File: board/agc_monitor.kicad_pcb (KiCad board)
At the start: 2 copper layers, 3 parts, among them J3 Conn_04x24, J4 Conn_04x24, P1 test_connector

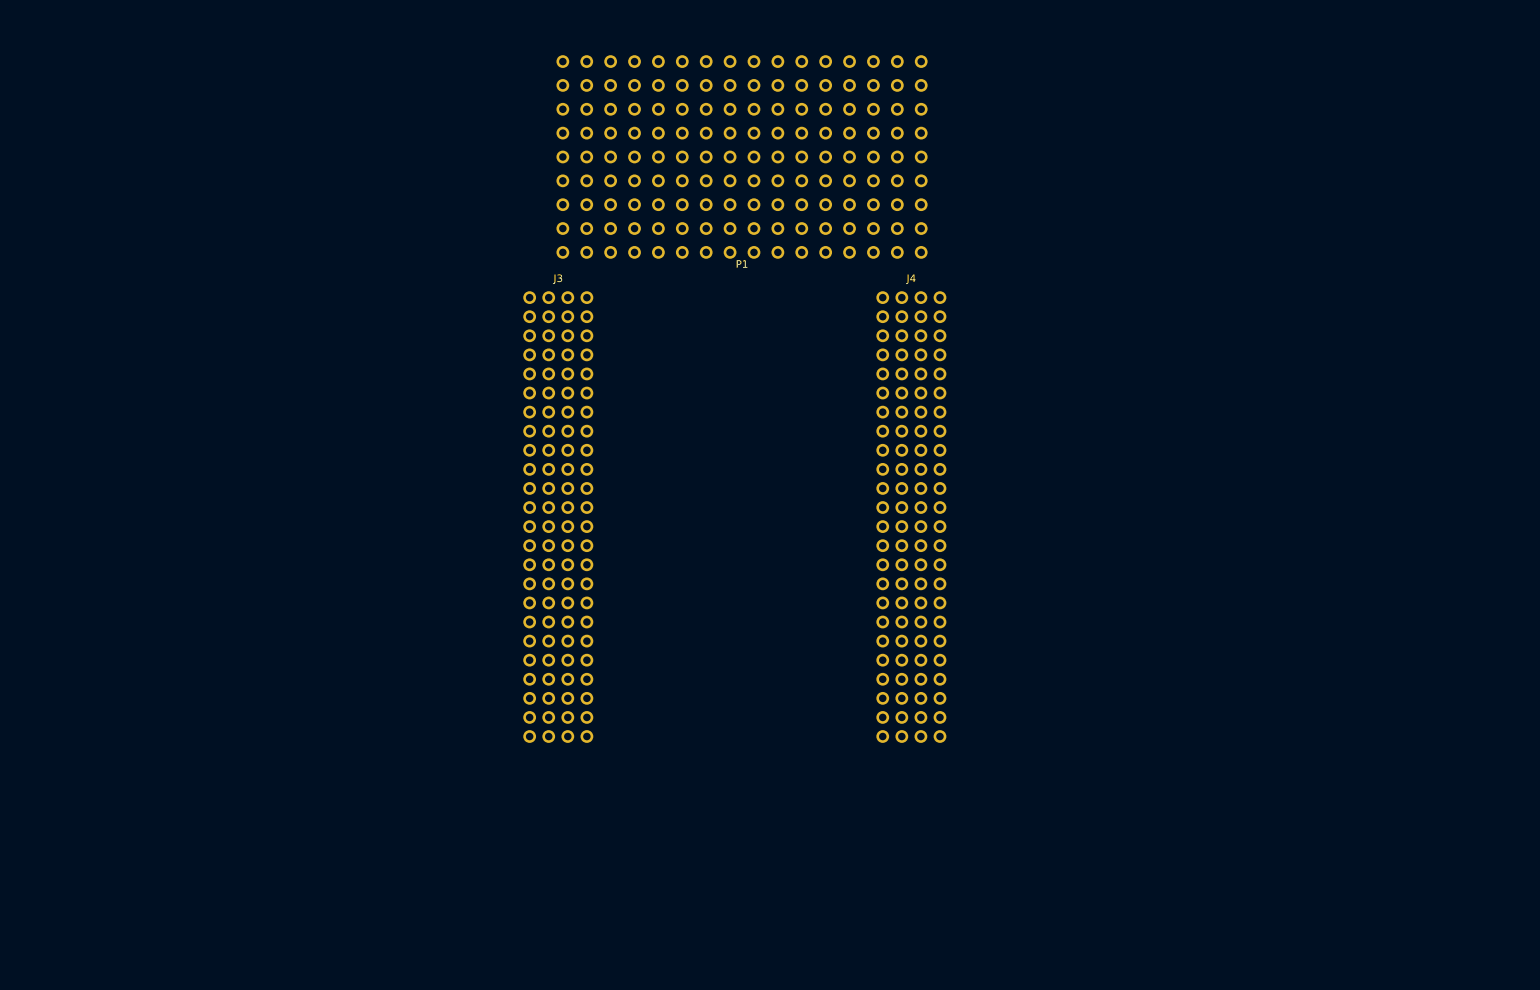
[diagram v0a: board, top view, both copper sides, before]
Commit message: Board: minor schematic tweaks, footprint creation, and initial subcircuit layout
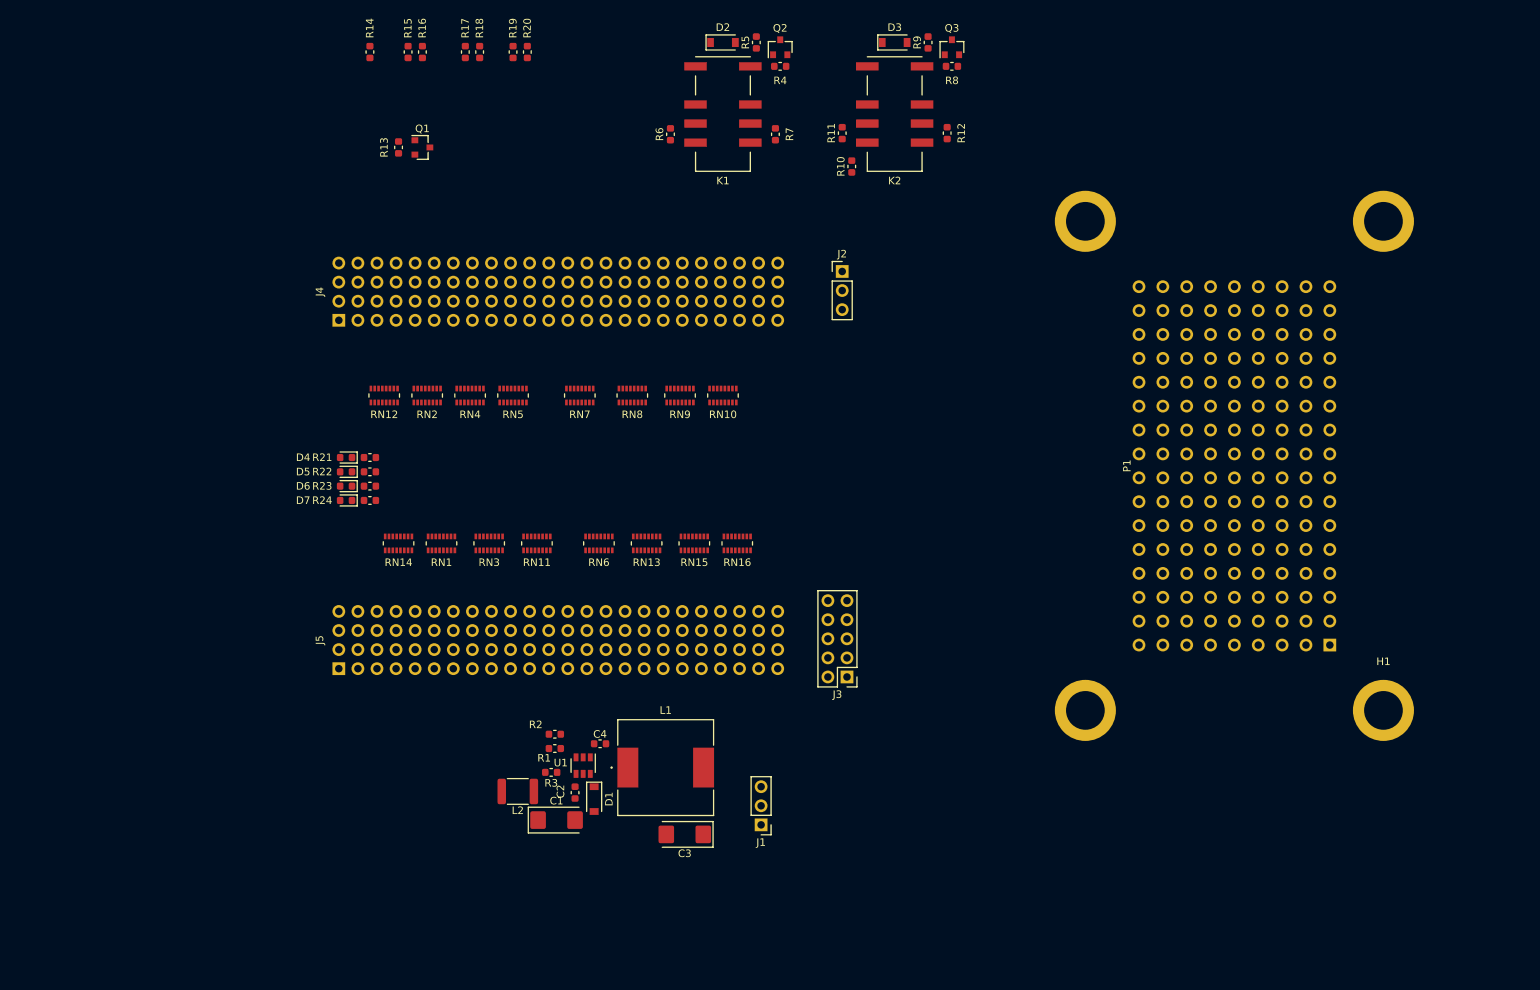
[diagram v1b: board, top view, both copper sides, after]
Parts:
- added C1: 6.8uF, Capacitor_Tantalum_SMD:CP_EIA-6032-28_Kemet-C, F.Cu at (99.8, 140.3)
- added C2: 4.7uF, Capacitor_SMD:C_0603_1608Metric, F.Cu at (102.2, 136.7)
- added C3: 22uF, Capacitor_Tantalum_SMD:CP_EIA-6032-28_Kemet-C, F.Cu at (116.8, 142.2)
- added C4: 100nF, Capacitor_SMD:C_0603_1608Metric, F.Cu at (105.6, 130.2)
- added D1: 30V,500mA, Diode_SMD:D_SOD-123, F.Cu at (104.8, 137.5)
- added D2: D_ALT, Diode_SMD:D_SOD-123, F.Cu at (121.9, 36.8)
- added D3: D_ALT, Diode_SMD:D_SOD-123, F.Cu at (144.8, 36.8)
- added D4: LED, LED_SMD:LED_0603_1608Metric, F.Cu at (71.8, 92.1)
- added D5: LED, LED_SMD:LED_0603_1608Metric, F.Cu at (71.8, 94.0)
- added D6: LED, LED_SMD:LED_0603_1608Metric, F.Cu at (71.8, 95.9)
- added D7: LED, LED_SMD:LED_0603_1608Metric, F.Cu at (71.8, 97.8)
- added H1: MountingHole_Pad, agc_monitor:MountingHole_1004579, F.Cu at (209.8, 125.7)
- added H2: MountingHole_Pad, agc_monitor:MountingHole_1004579, F.Cu at (170.2, 125.7)
- added H3: MountingHole_Pad, agc_monitor:MountingHole_1004579, F.Cu at (170.2, 60.6)
- added H4: MountingHole_Pad, agc_monitor:MountingHole_1004579, F.Cu at (209.8, 60.6)
- added J1: Conn_01x03, Connector_PinHeader_2.54mm:PinHeader_1x03_P2.54mm_Vertical, F.Cu at (127.0, 141.0)
- added J2: Conn_01x03, Connector_PinHeader_2.54mm:PinHeader_1x03_P2.54mm_Vertical, F.Cu at (137.8, 67.3)
- added J5: Styx_P5, agc_monitor:PinHeader_4x24_P2.54mm_Vertical, F.Cu at (100.0, 116.4)
- added K1: EE2-12NU, agc_monitor:Kemet-EE2, F.Cu at (121.9, 46.4)
- added K2: EE2-12NU, agc_monitor:Kemet-EE2, F.Cu at (144.8, 46.4)
- added L1: 68uH, agc_monitor:SRR1210-680M, F.Cu at (114.3, 133.3)
- added L2: 8.2uH, Inductor_SMD:L_1812_4532Metric, F.Cu at (94.6, 136.5)
- added Q1: MMBT3904, Package_TO_SOT_SMD:SOT-23, F.Cu at (81.9, 50.8)
- added Q2: MMBT3904, Package_TO_SOT_SMD:SOT-23, F.Cu at (129.5, 37.5)
- added Q3: MMBT3904, Package_TO_SOT_SMD:SOT-23, F.Cu at (152.4, 37.5)
- added R1: 28k, Resistor_SMD:R_0603_1608Metric, F.Cu at (99.5, 130.8)
- added R10: 3.3k, Resistor_SMD:R_0603_1608Metric, F.Cu at (139.1, 53.3)
- added R11: 0, Resistor_SMD:R_0603_1608Metric, F.Cu at (137.8, 48.9)
- added R12: 0, Resistor_SMD:R_0603_1608Metric, F.Cu at (151.8, 48.9)
- added R13: 1.5k, Resistor_SMD:R_0603_1608Metric, F.Cu at (78.7, 50.8)
- added R14: 1.2k, Resistor_SMD:R_0603_1608Metric, F.Cu at (74.9, 38.1)
- added R15: 4.7k, Resistor_SMD:R_0603_1608Metric, F.Cu at (80.0, 38.1)
- added R16: 1.5k, Resistor_SMD:R_0603_1608Metric, F.Cu at (81.9, 38.1)
- added R17: 4.7k, Resistor_SMD:R_0603_1608Metric, F.Cu at (87.6, 38.1)
- added R18: 1.2k, Resistor_SMD:R_0603_1608Metric, F.Cu at (89.5, 38.1)
- added R19: 22k, Resistor_SMD:R_0603_1608Metric, F.Cu at (94.0, 38.1)
- added R2: 8.45k, Resistor_SMD:R_0603_1608Metric, F.Cu at (99.5, 128.9)
- added R20: 1.5k, Resistor_SMD:R_0603_1608Metric, F.Cu at (95.9, 38.1)
- added R21: 330, Resistor_SMD:R_0603_1608Metric, F.Cu at (74.9, 92.1)
- added R22: 330, Resistor_SMD:R_0603_1608Metric, F.Cu at (74.9, 94.0)
- added R23: 330, Resistor_SMD:R_0603_1608Metric, F.Cu at (74.9, 95.9)
- added R24: 330, Resistor_SMD:R_0603_1608Metric, F.Cu at (74.9, 97.8)
- added R3: 0, Resistor_SMD:R_0603_1608Metric, F.Cu at (99.1, 134.0)
- added R4: 1.5k, Resistor_SMD:R_0603_1608Metric, F.Cu at (129.5, 40.0)
- added R5: 150, Resistor_SMD:R_0603_1608Metric, F.Cu at (126.4, 36.8)
- added R6: 0, Resistor_SMD:R_0603_1608Metric, F.Cu at (114.9, 49.0)
- added R7: 0, Resistor_SMD:R_0603_1608Metric, F.Cu at (128.9, 49.0)
- added R8: 1.5k, Resistor_SMD:R_0603_1608Metric, F.Cu at (152.4, 40.0)
- added R9: 150, Resistor_SMD:R_0603_1608Metric, F.Cu at (149.2, 36.8)
- added RN1: 3.3k, agc_monitor:EXB-2HV332JV, F.Cu at (84.5, 103.5)
- added RN10: 3.3k, agc_monitor:EXB-2HV332JV, F.Cu at (121.9, 83.8)
- added RN11: 3.3k, agc_monitor:EXB-2HV332JV, F.Cu at (97.2, 103.5)
- added RN12: 3.3k, agc_monitor:EXB-2HV332JV, F.Cu at (76.8, 83.8)
- added RN13: 3.3k, agc_monitor:EXB-2HV332JV, F.Cu at (111.8, 103.5)
- added RN14: 3.3k, agc_monitor:EXB-2HV332JV, F.Cu at (78.7, 103.5)
- added RN15: 3.3k, agc_monitor:EXB-2HV332JV, F.Cu at (118.1, 103.5)
- added RN16: 3.3k, agc_monitor:EXB-2HV332JV, F.Cu at (123.8, 103.5)
- added RN2: 3.3k, agc_monitor:EXB-2HV332JV, F.Cu at (82.5, 83.8)
- added RN3: 3.3k, agc_monitor:EXB-2HV332JV, F.Cu at (90.8, 103.5)
- added RN4: 3.3k, agc_monitor:EXB-2HV332JV, F.Cu at (88.3, 83.8)
- added RN5: 3.3k, agc_monitor:EXB-2HV332JV, F.Cu at (94.0, 83.8)
- added RN6: 3.3k, agc_monitor:EXB-2HV332JV, F.Cu at (105.4, 103.5)
- added RN7: 3.3k, agc_monitor:EXB-2HV332JV, F.Cu at (102.9, 83.8)
- added RN8: 3.3k, agc_monitor:EXB-2HV332JV, F.Cu at (109.9, 83.8)
- added RN9: 3.3k, agc_monitor:EXB-2HV332JV, F.Cu at (116.2, 83.8)
- added U1: LMR16006XDDC, Package_TO_SOT_SMD:SOT-23-6, F.Cu at (103.3, 133.1)
- J3: value Conn_04x24 -> Conn_01x10; footprint agc_monitor:PinHeader_4x24_P2.54mm_Vertical -> Connector_PinHeader_2.54mm:PinHeader_2x05_P2.54mm_Vertical
- J4: value Conn_04x24 -> Styx_P4
- moved P1 77.4 mm to (190.0, 93.2), turned to 270 degrees
- moved J4 55.8 mm to (100.0, 70.0), turned to 90 degrees
- moved J3 43.9 mm to (138.4, 121.3), turned to 180 degrees
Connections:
- J3 pad 1: Net-(J3-Pad1) -> +3V3_IO
- J3 pad 10: Net-(J3-Pad10) -> GND
- J3 pad 2: Net-(J3-Pad2) -> /StyxConnectors/DBG1
- J3 pad 3: Net-(J3-Pad3) -> /StyxConnectors/DBG2
- J3 pad 4: Net-(J3-Pad4) -> /StyxConnectors/DBG3
- J3 pad 5: Net-(J3-Pad5) -> /StyxConnectors/DBG4
- J3 pad 6: Net-(J3-Pad6) -> /StyxConnectors/DBG5
- J3 pad 7: Net-(J3-Pad7) -> /StyxConnectors/DBG6
- J3 pad 8: Net-(J3-Pad8) -> /StyxConnectors/DBG7
- J3 pad 9: Net-(J3-Pad9) -> /StyxConnectors/DBG8
- J4 pad 10: Net-(J4-Pad10) -> ADC_BPLSSW_P
- J4 pad 11: Net-(J4-Pad11) -> GND
- J4 pad 12: Net-(J4-Pad12) -> ADC_4SW_P
- J4 pad 13: Net-(J4-Pad13) -> MWCH
- J4 pad 14: Net-(J4-Pad14) -> MRCH
- J4 pad 15: Net-(J4-Pad15) -> GND
- J4 pad 16: Net-(J4-Pad16) -> MTLO
- J4 pad 17: Net-(J4-Pad17) -> MWL01
- J4 pad 18: Net-(J4-Pad18) -> MWL02
- J4 pad 19: Net-(J4-Pad19) -> MWL03
- J4 pad 2: Net-(J4-Pad2) -> +3V3_FPGA
- J4 pad 20: Net-(J4-Pad20) -> MWL04
- J4 pad 21: Net-(J4-Pad21) -> MWL05
- J4 pad 22: Net-(J4-Pad22) -> MWL06
- J4 pad 23: Net-(J4-Pad23) -> MWL07
- J4 pad 24: Net-(J4-Pad24) -> MWL08
- J4 pad 25: Net-(J4-Pad25) -> MWL09
- J4 pad 26: Net-(J4-Pad26) -> MWL10
- J4 pad 27: Net-(J4-Pad27) -> MWL11
- J4 pad 28: Net-(J4-Pad28) -> MWL12
- J4 pad 29: Net-(J4-Pad29) -> MWL13
- J4 pad 30: Net-(J4-Pad30) -> MWL14
- J4 pad 31: Net-(J4-Pad31) -> MWL15
- J4 pad 32: Net-(J4-Pad32) -> MWL16
- J4 pad 33: Net-(J4-Pad33) -> MT01
- J4 pad 34: Net-(J4-Pad34) -> MT02
- J4 pad 35: Net-(J4-Pad35) -> MT03
- J4 pad 36: Net-(J4-Pad36) -> MT04
- J4 pad 37: Net-(J4-Pad37) -> MT05
- J4 pad 38: Net-(J4-Pad38) -> MT06
- J4 pad 39: Net-(J4-Pad39) -> MT07
- J4 pad 4: Net-(J4-Pad4) -> GND
- J4 pad 40: Net-(J4-Pad40) -> MT08
- J4 pad 41: Net-(J4-Pad41) -> MT09
- J4 pad 42: Net-(J4-Pad42) -> MT10
- J4 pad 43: Net-(J4-Pad43) -> MT11
- J4 pad 44: Net-(J4-Pad44) -> MT12
- J4 pad 45: Net-(J4-Pad45) -> Net-(J4-Pad1)
- J4 pad 46: Net-(J4-Pad46) -> ADC_3V3_P
- J4 pad 47: Net-(J4-Pad47) -> /StyxConnectors/DBG1
- J4 pad 48: Net-(J4-Pad48) -> /StyxConnectors/DBG2
- J4 pad 49: Net-(J4-Pad49) -> Net-(J4-Pad1)
- J4 pad 5: Net-(J4-Pad5) -> MWG
- J4 pad 50: Net-(J4-Pad50) -> GND
- J4 pad 51: Net-(J4-Pad51) -> GND
- J4 pad 52: Net-(J4-Pad52) -> GND
- J4 pad 53: Net-(J4-Pad53) -> MST1
- J4 pad 54: Net-(J4-Pad54) -> MST2
- J4 pad 55: Net-(J4-Pad55) -> MST3
- J4 pad 56: Net-(J4-Pad56) -> MTCSA_n
- J4 pad 57: Net-(J4-Pad57) -> MWSG
- J4 pad 58: Net-(J4-Pad58) -> MWZG
- J4 pad 59: Net-(J4-Pad59) -> MWYG
- J4 pad 6: Net-(J4-Pad6) -> MNISQ
- J4 pad 60: Net-(J4-Pad60) -> MWQG
- J4 pad 61: Net-(J4-Pad61) -> MWBG
- J4 pad 62: Net-(J4-Pad62) -> MSQ10
- J4 pad 63: Net-(J4-Pad63) -> MSQ11
- J4 pad 64: Net-(J4-Pad64) -> MSQ12
- J4 pad 65: Net-(J4-Pad65) -> MSQ13
- J4 pad 66: Net-(J4-Pad66) -> MSQ14
- J4 pad 67: Net-(J4-Pad67) -> MSQEXT
- J4 pad 68: Net-(J4-Pad68) -> MSQ16
- J4 pad 69: Net-(J4-Pad69) -> MBR1
- J4 pad 7: Net-(J4-Pad7) -> MREQIN
- J4 pad 70: Net-(J4-Pad70) -> MBR2
- J4 pad 71: Net-(J4-Pad71) -> MIIP
- J4 pad 72: Net-(J4-Pad72) -> MCTRAL_n
- J4 pad 73: Net-(J4-Pad73) -> MTCAL_n
- J4 pad 74: Net-(J4-Pad74) -> MRPTAL_n
- J4 pad 75: Net-(J4-Pad75) -> MPAL_n
- J4 pad 76: Net-(J4-Pad76) -> MSTPIT_n
- J4 pad 77: Net-(J4-Pad77) -> MGOJAM
- J4 pad 78: Net-(J4-Pad78) -> MINHL
- J4 pad 79: Net-(J4-Pad79) -> MINKL
- J4 pad 8: Net-(J4-Pad8) -> MWATCH_n
- J4 pad 80: Net-(J4-Pad80) -> MWLG
- J4 pad 81: Net-(J4-Pad81) -> MONWT
- J4 pad 82: Net-(J4-Pad82) -> MRSC
- J4 pad 83: Net-(J4-Pad83) -> MRLG
- J4 pad 84: Net-(J4-Pad84) -> MGP_n
- J4 pad 85: Net-(J4-Pad85) -> MSP
- J4 pad 86: Net-(J4-Pad86) -> MRGG
- J4 pad 87: Net-(J4-Pad87) -> MWAG
- J4 pad 88: Net-(J4-Pad88) -> MRAG
- J4 pad 89: Net-(J4-Pad89) -> GND
- J4 pad 9: Net-(J4-Pad9) -> Net-(J4-Pad1)
- J4 pad 90: Net-(J4-Pad90) -> GND
- J4 pad 91: Net-(J4-Pad91) -> GND
- J4 pad 92: Net-(J4-Pad92) -> GND
- J4 pad 93: Net-(J4-Pad93) -> +3V3_FPGA
- J4 pad 94: Net-(J4-Pad94) -> +3V3_FPGA
- J4 pad 95: Net-(J4-Pad95) -> +3V3_FPGA
- J4 pad 96: Net-(J4-Pad96) -> +3V3_FPGA
- P1 pad 101: Net-(P1-Pad101) -> MDT01
- P1 pad 102: Net-(P1-Pad102) -> MDT02
- P1 pad 103: Net-(P1-Pad103) -> MDT03
- P1 pad 104: Net-(P1-Pad104) -> MDT04
- P1 pad 105: Net-(P1-Pad105) -> MDT05
- P1 pad 106: Net-(P1-Pad106) -> MDT06
- P1 pad 107: Net-(P1-Pad107) -> MDT07
- P1 pad 108: Net-(P1-Pad108) -> MDT08
- P1 pad 109: Net-(P1-Pad109) -> MDT09
- P1 pad 110: Net-(P1-Pad110) -> MDT10
- P1 pad 111: Net-(P1-Pad111) -> MDT11
- P1 pad 112: Net-(P1-Pad112) -> MDT12
- P1 pad 113: Net-(P1-Pad113) -> MDT13
- P1 pad 114: Net-(P1-Pad114) -> MDT14
- P1 pad 115: Net-(P1-Pad115) -> MDT15
- P1 pad 116: Net-(P1-Pad116) -> MDT16
- P1 pad 201: Net-(P1-Pad201) -> MWL01
- P1 pad 202: Net-(P1-Pad202) -> MWL02
- P1 pad 203: Net-(P1-Pad203) -> MWL03
- P1 pad 204: Net-(P1-Pad204) -> MWL04
- P1 pad 205: Net-(P1-Pad205) -> MWL05
- P1 pad 206: Net-(P1-Pad206) -> MWL06
- P1 pad 207: Net-(P1-Pad207) -> MWL07
- P1 pad 208: Net-(P1-Pad208) -> MWL08
- P1 pad 209: Net-(P1-Pad209) -> MWL09
- P1 pad 210: Net-(P1-Pad210) -> MWL10
- P1 pad 211: Net-(P1-Pad211) -> MWL11
- P1 pad 212: Net-(P1-Pad212) -> MWL12
- P1 pad 213: Net-(P1-Pad213) -> MWL13
- P1 pad 214: Net-(P1-Pad214) -> MWL14
- P1 pad 215: Net-(P1-Pad215) -> MWL15
- P1 pad 216: Net-(P1-Pad216) -> MWL16
- P1 pad 301: Net-(P1-Pad301) -> MT01
- P1 pad 302: Net-(P1-Pad302) -> MT02
- P1 pad 303: Net-(P1-Pad303) -> MT03
- P1 pad 304: Net-(P1-Pad304) -> MT04
- P1 pad 305: Net-(P1-Pad305) -> MT05
- P1 pad 306: Net-(P1-Pad306) -> MT06
- P1 pad 307: Net-(P1-Pad307) -> MT07
- P1 pad 308: Net-(P1-Pad308) -> MT08
- P1 pad 309: Net-(P1-Pad309) -> MT09
- P1 pad 310: Net-(P1-Pad310) -> MT10
- P1 pad 311: Net-(P1-Pad311) -> MT11
- P1 pad 312: Net-(P1-Pad312) -> MT12
- P1 pad 313: Net-(P1-Pad313) -> MRULOG
- P1 pad 314: Net-(P1-Pad314) -> MWFBG
- P1 pad 315: Net-(P1-Pad315) -> MWEBG
- P1 pad 316: Net-(P1-Pad316) -> MWBBEG
- P1 pad 401: Net-(P1-Pad401) -> MST1
- P1 pad 402: Net-(P1-Pad402) -> MST2
- P1 pad 403: Net-(P1-Pad403) -> MST3
- P1 pad 404: Net-(P1-Pad404) -> MTCSA_n
- P1 pad 405: Net-(P1-Pad405) -> MWSG
- P1 pad 406: Net-(P1-Pad406) -> MWZG
- P1 pad 407: Net-(P1-Pad407) -> MWYG
- P1 pad 408: Net-(P1-Pad408) -> MWQG
- P1 pad 409: Net-(P1-Pad409) -> MWBG
- P1 pad 410: Net-(P1-Pad410) -> MSQ10
- P1 pad 411: Net-(P1-Pad411) -> MSQ11
- P1 pad 412: Net-(P1-Pad412) -> MSQ12
- P1 pad 413: Net-(P1-Pad413) -> MSQ13
- P1 pad 414: Net-(P1-Pad414) -> MSQ14
- P1 pad 415: Net-(P1-Pad415) -> MSQEXT
- P1 pad 416: Net-(P1-Pad416) -> MSQ16
- P1 pad 501: Net-(P1-Pad501) -> MBR1
- P1 pad 502: Net-(P1-Pad502) -> MBR2
- P1 pad 503: Net-(P1-Pad503) -> MIIP
- P1 pad 504: Net-(P1-Pad504) -> MCTRAL_n
- P1 pad 505: Net-(P1-Pad505) -> MTCAL_n
- P1 pad 506: Net-(P1-Pad506) -> MRPTAL_n
- P1 pad 507: Net-(P1-Pad507) -> ALGA
- P1 pad 508: Net-(P1-Pad508) -> MPAL_n
- P1 pad 509: Net-(P1-Pad509) -> MSTPIT_n
- P1 pad 510: Net-(P1-Pad510) -> MGOJAM
- P1 pad 511: Net-(P1-Pad511) -> MINHL
- P1 pad 512: Net-(P1-Pad512) -> MINKL
- P1 pad 513: Net-(P1-Pad513) -> MWLG
- P1 pad 514: Net-(P1-Pad514) -> MONWT
- P1 pad 515: Net-(P1-Pad515) -> MRSC
- P1 pad 516: Net-(P1-Pad516) -> MRLG
- P1 pad 601: Net-(P1-Pad601) -> STRT1
- P1 pad 602: Net-(P1-Pad602) -> STRT2
- P1 pad 603: Net-(P1-Pad603) -> MNHSBF
- P1 pad 604: Net-(P1-Pad604) -> MNHNC
- P1 pad 605: Net-(P1-Pad605) -> MNHRPT
- P1 pad 606: Net-(P1-Pad606) -> MTCSAI
- P1 pad 607: Net-(P1-Pad607) -> MSTRT
- P1 pad 608: Net-(P1-Pad608) -> MSTP
- P1 pad 609: Net-(P1-Pad609) -> MSBSTP
- P1 pad 610: Net-(P1-Pad610) -> MRDCH
- P1 pad 611: Net-(P1-Pad611) -> MLDCH
- P1 pad 612: Net-(P1-Pad612) -> MGP_n
- P1 pad 613: Net-(P1-Pad613) -> MSP
- P1 pad 614: Net-(P1-Pad614) -> MRGG
- P1 pad 615: Net-(P1-Pad615) -> MWAG
- P1 pad 616: Net-(P1-Pad616) -> MRAG
- P1 pad 701: Net-(P1-Pad701) -> CTRL1
- P1 pad 702: Net-(P1-Pad702) -> CTRL2
- P1 pad 703: Net-(P1-Pad703) -> +3V3_IO
- P1 pad 704: Net-(P1-Pad704) -> MTLO
- P1 pad 705: Net-(P1-Pad705) -> MWCH
- P1 pad 706: Net-(P1-Pad706) -> MRCH
- P1 pad 707: Net-(P1-Pad707) -> MONPAR
- P1 pad 708: Net-(P1-Pad708) -> MONWBK
- P1 pad 709: Net-(P1-Pad709) -> MWG
- P1 pad 710: Net-(P1-Pad710) -> MNISQ
- P1 pad 711: Net-(P1-Pad711) -> MREQIN
- P1 pad 712: Net-(P1-Pad712) -> MWATCH_n
- P1 pad 713: Net-(P1-Pad713) -> MLOAD
- P1 pad 714: Net-(P1-Pad714) -> MREAD
- P1 pad 715: Net-(P1-Pad715) -> MON800
- P1 pad 716: Net-(P1-Pad716) -> MPIPAL_n
- P1 pad 801: Net-(P1-Pad801) -> BPLSSW
- P1 pad 802: Net-(P1-Pad802) -> +4SW
- P1 pad 803: Net-(P1-Pad803) -> MSP803
- P1 pad 804: Net-(P1-Pad804) -> SIGNY
- P1 pad 805: Net-(P1-Pad805) -> MSP805
- P1 pad 806: Net-(P1-Pad806) -> MSP806
- P1 pad 807: Net-(P1-Pad807) -> MSP807
- P1 pad 808: Net-(P1-Pad808) -> MSCDBL_n
- P1 pad 809: Net-(P1-Pad809) -> NHALGA
- P1 pad 810: Net-(P1-Pad810) -> DOSCAL
- P1 pad 811: Net-(P1-Pad811) -> DBLTST
- P1 pad 812: Net-(P1-Pad812) -> MWARNF_n
- P1 pad 813: Net-(P1-Pad813) -> OUTCOM
- P1 pad 814: Net-(P1-Pad814) -> MSCAFL_n
- P1 pad 815: Net-(P1-Pad815) -> MOSCAL_n
- P1 pad 816: Net-(P1-Pad816) -> MVFAIL_n
- P1 pad 902: Net-(P1-Pad902) -> MSP902
- P1 pad 904: Net-(P1-Pad904) -> MSP904
- P1 pad 906: Net-(P1-Pad906) -> MAMU
- P1 pad 908: Net-(P1-Pad908) -> MSP908
- P1 pad 910: Net-(P1-Pad910) -> MSP910
- P1 pad 912: Net-(P1-Pad912) -> MSP912
- P1 pad 914: Net-(P1-Pad914) -> MSP914
- P1 pad 916: Net-(P1-Pad916) -> MSP916
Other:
- net class Default: clearance 0.2 -> 0.2032; trace_width 0.25 -> 0.2032
- rule trace_clearance: 0.2 -> 0.2032

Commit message: Board: minor redesign and initial ideas for layout
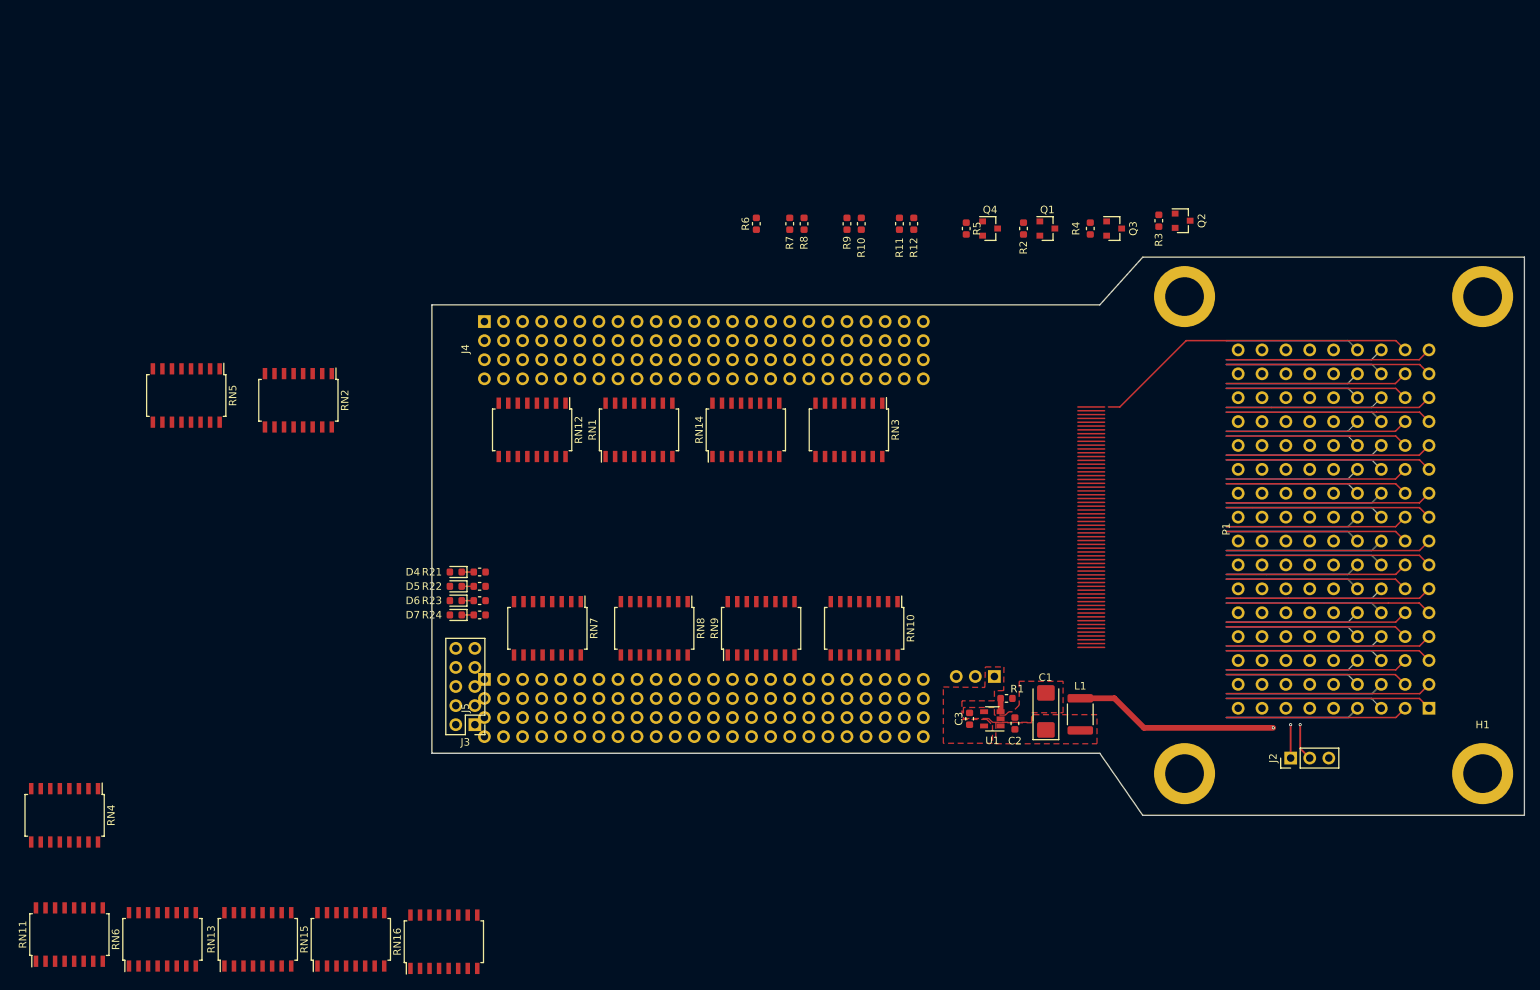
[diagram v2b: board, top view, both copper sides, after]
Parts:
- removed C4: 100nF, Capacitor_SMD:C_0603_1608Metric
- removed D1: 30V,500mA, Diode_SMD:D_SOD-123
- removed D2, D3: D_ALT, Diode_SMD:D_SOD-123
- removed K1, K2: EE2-12NU, agc_monitor:Kemet-EE2
- removed L2: 8.2uH, Inductor_SMD:L_1812_4532Metric
- removed R13, R16, R20: 1.5k, Resistor_SMD:R_0603_1608Metric
- removed R14, R18: 1.2k, Resistor_SMD:R_0603_1608Metric
- removed R15, R17: 4.7k, Resistor_SMD:R_0603_1608Metric
- removed R19: 22k, Resistor_SMD:R_0603_1608Metric
- added Q4: MMBT3904, Package_TO_SOT_SMD:SOT-23, F.Cu at (157.5, 61.6)
- C1: value 6.8uF -> 12uF
- C2: value 4.7uF -> 0.1uF
- C3: value 22uF -> 0.1uF; footprint Capacitor_Tantalum_SMD:CP_EIA-6032-28_Kemet-C -> Capacitor_SMD:C_0603_1608Metric
- J1, J4, J5: moved to B.Cu
- L1: value 68uH -> 8.2uH; footprint agc_monitor:SRR1210-680M -> Inductor_SMD:L_1812_4532Metric
- R1: value 28k -> 10k
- R10: value 3.3k -> 1.2k
- R11: value 0 -> 22k
- R12, R3: value 0 -> 1.5k
- R2: value 8.45k -> 1.5k
- R5: value 150 -> 1.5k
- R6: value 0 -> 1.2k
- R7: value 0 -> 4.7k
- R9: value 150 -> 4.7k
- RN1, RN10, RN11, RN12, RN13, RN14, RN15, RN16, RN2, RN3, RN4, RN5, RN6, RN7, RN8, RN9: footprint agc_monitor:EXB-2HV332JV -> Package_SO:SOIC-16W_5.3x10.2mm_P1.27mm
- U1: value LMR16006XDDC -> TLV73333P_SOT23-5; footprint Package_TO_SOT_SMD:SOT-23-6 -> Package_TO_SOT_SMD:SOT-23-5
- moved R3 109.2 mm to (179.9, 60.6), turned to 270 degrees
- moved R2 91.8 mm to (161.9, 61.6), turned to 270 degrees
- moved J2 88.1 mm to (197.5, 132.1), turned to 90 degrees
- moved Q1 83.9 mm to (165.1, 61.6)
- moved RN11 81.1 mm to (34.9, 155.6)
- moved RN6 78.4 mm to (47.3, 156.2)
- moved RN4 77.7 mm to (34.3, 139.7)
- moved RN13 73.9 mm to (60.0, 156.2)
- moved RN15 69.8 mm to (72.4, 156.2)
- moved C1 66.7 mm to (164.9, 125.9), turned to 90 degrees
- moved RN16 65.9 mm to (84.8, 156.5)
- moved R1 60.5 mm to (159.7, 124.1), turned to 180 degrees
- moved C2 59.3 mm to (160.8, 127.5), turned to 90 degrees
- moved Q2 58.3 mm to (183.1, 60.6), turned to 0 degrees
- moved L1 55.6 mm to (169.5, 126.3), turned to 270 degrees
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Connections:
- J5 pad 20: Net-(J5-Pad20) -> NHSTRT2
- J5 pad 85: NHALGA_R -> NHALGA
- J5 pad 86: NHSTRT_R -> NHSTRT1
- L1 pad 1: Net-(C4-Pad1) -> +4SW
- L1 pad 2: +3V3_AGC -> Net-(C1-Pad1)
- Q1 pad 3: SIGNY_n -> STRT1
- Q2 pad 3: Net-(Q2-Pad3) -> STRT2
- Q3 pad 3: Net-(Q3-Pad3) -> ALGA
- R1 pad 1: +3V3_AGC -> +3V3_FPGA
- R1 pad 2: Net-(R1-Pad2) -> EN_3V3_AGC
- R10 pad 1: +3V3_IO -> ADC_4SW_P
- R10 pad 2: Net-(K2-Pad5) -> GND
- R11 pad 1: NHALGA -> BPLSSW
- R11 pad 2: Net-(K2-Pad4) -> ADC_BPLSSW_P
- R12 pad 1: ALGA -> ADC_BPLSSW_P
- R12 pad 2: Net-(K2-Pad9) -> GND
- R2 pad 1: Net-(R1-Pad2) -> Net-(Q1-Pad1)
- R2 pad 2: GND -> NHSTRT1
- R3 pad 1: Net-(R3-Pad1) -> Net-(Q2-Pad1)
- R3 pad 2: EN_3V3_AGC -> NHSTRT2
- R4 pad 1: Net-(Q2-Pad1) -> Net-(Q3-Pad1)
- R4 pad 2: NHSTRT_R -> NHALGA
- R5 pad 2: Net-(Q2-Pad3) -> SIGNY
- R6 pad 1: STRT1 -> MTLO
- R6 pad 2: Net-(K1-Pad4) -> GND
- R7 pad 1: STRT2 -> +3V3_IO
- R7 pad 2: Net-(K1-Pad9) -> ADC_3V3_P
- R8 pad 1: Net-(Q3-Pad1) -> ADC_3V3_P
- R8 pad 2: NHALGA_R -> GND
- R9 pad 1: Net-(D3-Pad2) -> +4SW
- R9 pad 2: Net-(Q3-Pad3) -> ADC_4SW_P
- U1 pad 1: Net-(C4-Pad2) -> Net-(C1-Pad1)
- U1 pad 3: Net-(R1-Pad2) -> EN_3V3_AGC
- U1 pad 4: Net-(R3-Pad1) -> GND
- U1 pad 5: Net-(C1-Pad1) -> +3V3_AGC
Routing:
- net (no net): track 0.00 -> 227.6 mm
- net MWL16: track 0.00 -> 43.7 mm
- net +4SW: track 0.00 -> 39.0 mm, vias 0 -> 1
- net MDT01: track 0.00 -> 27.6 mm
- net MDT16: track 0.00 -> 27.5 mm
- net MDT14: track 0.00 -> 27.5 mm
- net MDT03: track 0.00 -> 27.5 mm
- net MDT12: track 0.00 -> 27.5 mm
- net MDT05: track 0.00 -> 27.5 mm
- net MDT10: track 0.00 -> 27.5 mm
- net MDT07: track 0.00 -> 27.5 mm
- net MDT09: track 0.00 -> 27.5 mm
- net MDT08: track 0.00 -> 27.5 mm
- net MDT11: track 0.00 -> 27.5 mm
- net MDT06: track 0.00 -> 27.5 mm
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- added copper zone on F.Cu, net +3V3_AGC
- added copper zone on In2.Cu, net +3V3_FPGA
- added copper zone on F.Cu, net GND
- added copper zone on In1.Cu, net GND
- added copper zone on F.Cu, net Net-(C1-Pad1)
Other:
- board outline added: 145.4 x 74.3 mm
- copper layers 2 -> 4
- net class 10Mil added: clearance 0.254, trace_width 0.254, via_dia 0.508, via_drill 0.254
- net class Default: clearance 0.2032 -> 0.254; via_dia 0.8 -> 0.4064; via_drill 0.4 -> 0.2032
- rule trace_clearance: 0.2032 -> 0.254
- rule trace_min: 0.2 -> 0.2032
- rule via_min_drill: 0.3 -> 0.2032
- rule via_min_size: 0.4 -> 0.4064

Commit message: Board: a bit more layout work on TC breakout
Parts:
- RN11, RN13, RN15, RN16, RN2, RN4, RN5, RN6: moved to B.Cu
- moved RN11 114.2 mm to (141.6, 114.9), turned to 270 degrees
- moved RN4 91.6 mm to (110.5, 88.9), turned to 90 degrees
- moved RN5 75.4 mm to (125.7, 88.9), turned to 90 degrees
- moved RN2 75.1 mm to (140.3, 88.9), turned to 90 degrees
- moved RN15 69.0 mm to (127.6, 114.9), turned to 270 degrees
- moved RN16 68.5 mm to (95.9, 88.9), turned to 270 degrees
- moved RN13 67.7 mm to (113.7, 114.9), turned to 270 degrees
- moved RN6 66.2 mm to (99.1, 114.9), turned to 270 degrees
- moved D5 5.12 mm to (81.3, 108.6)
- moved D6 5.12 mm to (81.3, 110.5)
- moved D7 5.12 mm to (81.3, 112.4)
- moved R22 5.12 mm to (84.5, 108.6)
- moved R23 5.12 mm to (84.5, 110.5)
- moved R24 5.12 mm to (84.5, 112.4)
- moved D4 5.12 mm to (81.3, 106.7)
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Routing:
- net (no net): track 227.6 -> 113.8 mm
- net MDT11: track 27.5 -> 58.0 mm
- net MDT10: track 27.5 -> 57.3 mm
- net MDT09: track 27.5 -> 56.9 mm
- net MDT12: track 27.5 -> 56.0 mm
- net MSP912: track 0.00 -> 20.7 mm
- net MWL16: track 43.7 -> 23.1 mm
- net MWARNF_n: track 5.28 -> 24.8 mm, vias 0 -> 1
- net MGP_n: track 11.6 -> 31.1 mm, vias 0 -> 1
- net MWL13: track 24.3 -> 43.8 mm
- net MSQ13: track 18.0 -> 37.5 mm
- net MSP910: track 0.00 -> 19.4 mm
- net MWL12: track 24.3 -> 43.7 mm
- net MSQ12: track 18.0 -> 37.3 mm
- net MWATCH_n: track 8.47 -> 27.7 mm, vias 0 -> 1
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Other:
- board size 145.4 x 74.3 mm -> 149.9 x 74.3 mm
- net class Default: clearance 0.254 -> 0.1524; trace_width 0.2032 -> 0.1524; via_dia 0.4064 -> 0.6096; via_drill 0.2032 -> 0.3048
- rule trace_clearance: 0.254 -> 0.1524
- rule trace_min: 0.2032 -> 0.1524
